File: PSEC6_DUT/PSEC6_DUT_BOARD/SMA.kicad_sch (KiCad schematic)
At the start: 0 parts

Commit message: schematic stuff
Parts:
- added C58, C59, C60, C61, C62, C63, C64, C65, C66, C67, C68, C69, C70, C71, C72, C73: 100n, Capacitor_SMD:C_0603_1608Metric, symbol Device:C_Small
- added J10, J3, J4, J5, J6, J7, J8, J9: Conn_Coaxial, Connector_Coaxial:SMA_Amphenol_132134-14_Vertical, symbol Connector:Conn_Coaxial
- added L1, L2, L3, L4, L5, L6, L7, L8: L, symbol Device:L
- added R50, R51, R52, R53, R54, R55, R56, R57: 50, Resistor_SMD:R_0603_1608Metric, symbol Device:R_Small_US
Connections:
- new net: C70.2, J9.2 (Ext)
- new net: C64.2, J6.2 (Ext)
- new net: C60.2, J4.2 (Ext)
- new net: C67.2, L5.1, R54.2
- new net: C62.2, J5.2 (Ext)
- new net: C59.2, L1.1, R50.2
- new net: C58.2, J3.2 (Ext)
- new net: C69.2, L6.1, R55.2
- new net: C71.2, L7.1, R56.2
- new net: C72.2, J10.2 (Ext)
- new net: C63.2, L3.1, R52.2
- new net: C65.2, L4.1, R53.2
- new net: C61.2, L2.1, R51.2
- new net: C68.2, J8.2 (Ext)
- new net: C73.2, L8.1, R57.2
- new net: C66.2, J7.2 (Ext)
- new net GND: C59.1, C61.1, C63.1, C65.1, C67.1, C69.1, C71.1, C73.1, J10.1 (In), J3.1 (In), J4.1 (In), J5.1 (In), J6.1 (In), J7.1 (In), J8.1 (In), J9.1 (In)
- new net SIGNAL1: C58.1, R50.1
- new net SIGNAL2: C60.1, C72.1, R51.1, R57.1
- new net SIGNAL3: C62.1, R52.1
- new net SIGNAL4: C64.1, R53.1
- new net SIGNAL5: C66.1, R54.1
- new net SIGNAL6: C68.1, R55.1
- new net SIGNAL7: C70.1, R56.1
- new net V_ped1: L1.2
- new net V_ped2: L2.2
- new net V_ped3: L3.2
- new net V_ped4: L4.2
- new net V_ped5: L5.2
- new net V_ped6: L6.2
- new net V_ped7: L7.2
- new net V_ped8: L8.2

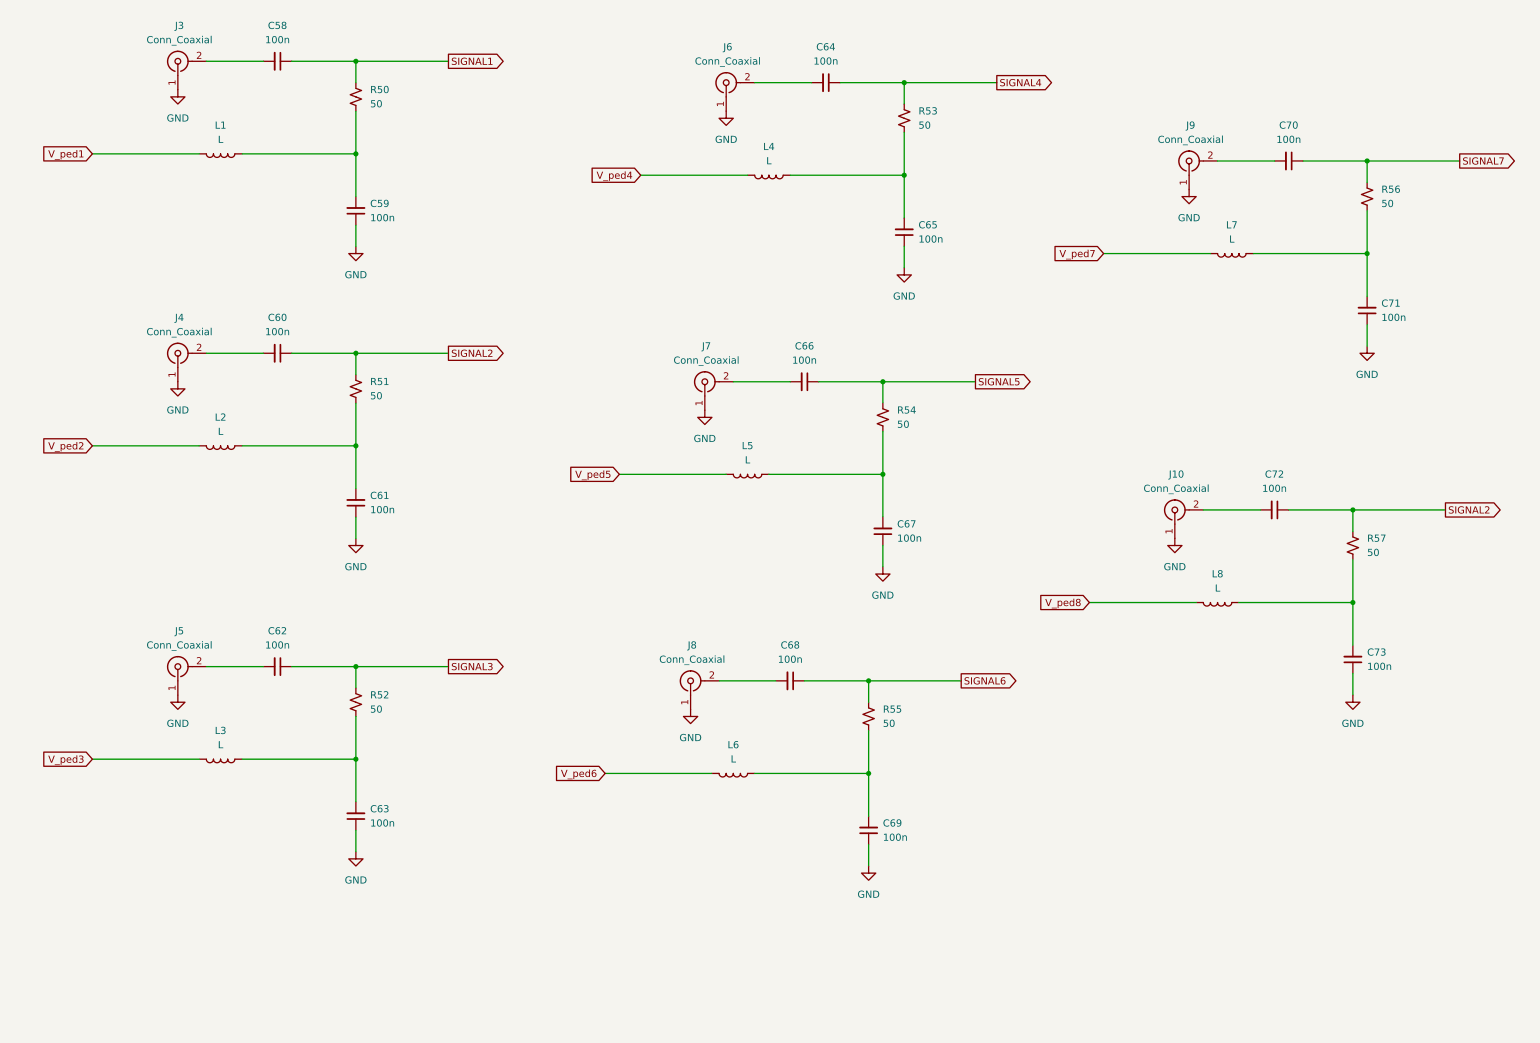
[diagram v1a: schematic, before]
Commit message: Updating values and added RC filters for DUT Card
Added RC filters onto the bias signals and discriminator thresholds, and added RCL values for the SMA devices to provide good DC biasing voltage from the pedestals.
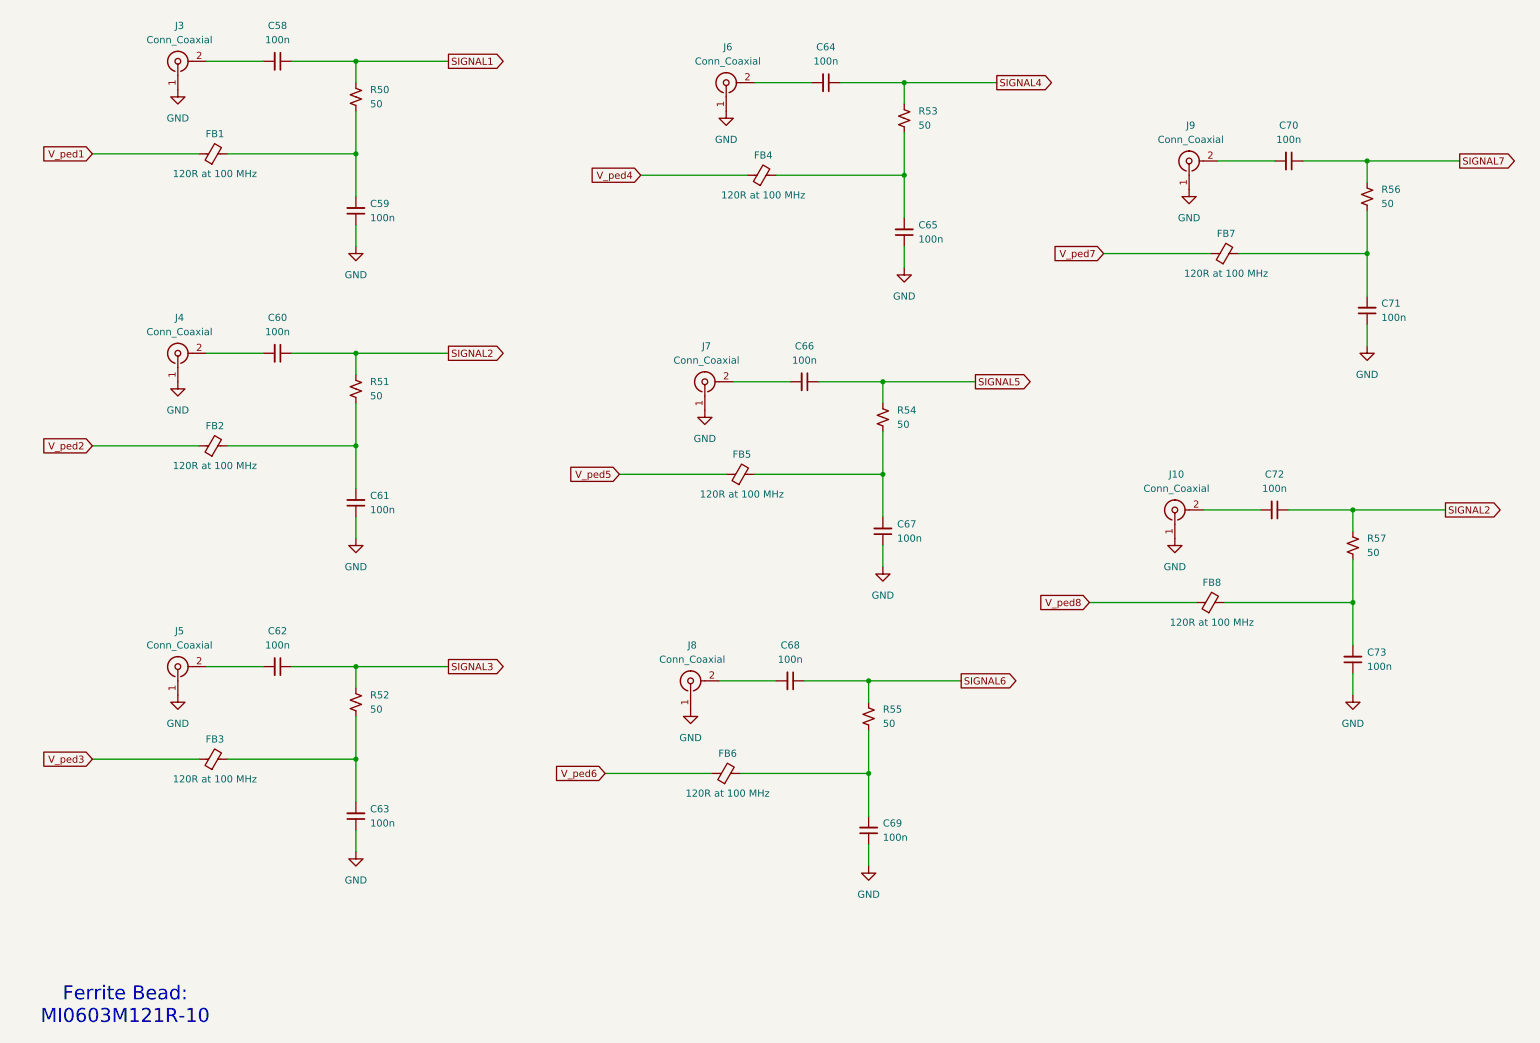
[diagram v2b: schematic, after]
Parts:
- removed L1, L2, L3, L4, L5, L6, L7, L8: L, symbol Device:L
- added FB1, FB2, FB3, FB4, FB5, FB6, FB7, FB8: 120R at 100 MHz, Resistor_SMD:R_0603_1608Metric, symbol Device:FerriteBead_Small
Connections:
- net V_ped1: now also FB1.1
- net V_ped2: now also FB2.1
- net V_ped3: now also FB3.1
- net V_ped4: now also FB4.1
- net V_ped5: now also FB5.1
- net V_ped6: now also FB6.1
- net V_ped7: now also FB7.1
- net V_ped8: now also FB8.1
- net at C67.2, R54.2: now also FB5.2
- net at C59.2, R50.2: now also FB1.2
- net at C69.2, R55.2: now also FB6.2
- net at C71.2, R56.2: now also FB7.2
- net at C63.2, R52.2: now also FB3.2
- net at C65.2, R53.2: now also FB4.2
- net at C61.2, R51.2: now also FB2.2
- net at C73.2, R57.2: now also FB8.2
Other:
- note added: "Ferrite Bead: MI0603M121R-10"

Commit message: DUT Board Schematic Done besides SAMTEC
The DUT Board is now done and fully documented besides the placement of the signals on the SAMTEC connector between the two boards, as the position of each connection will be determined during layout.
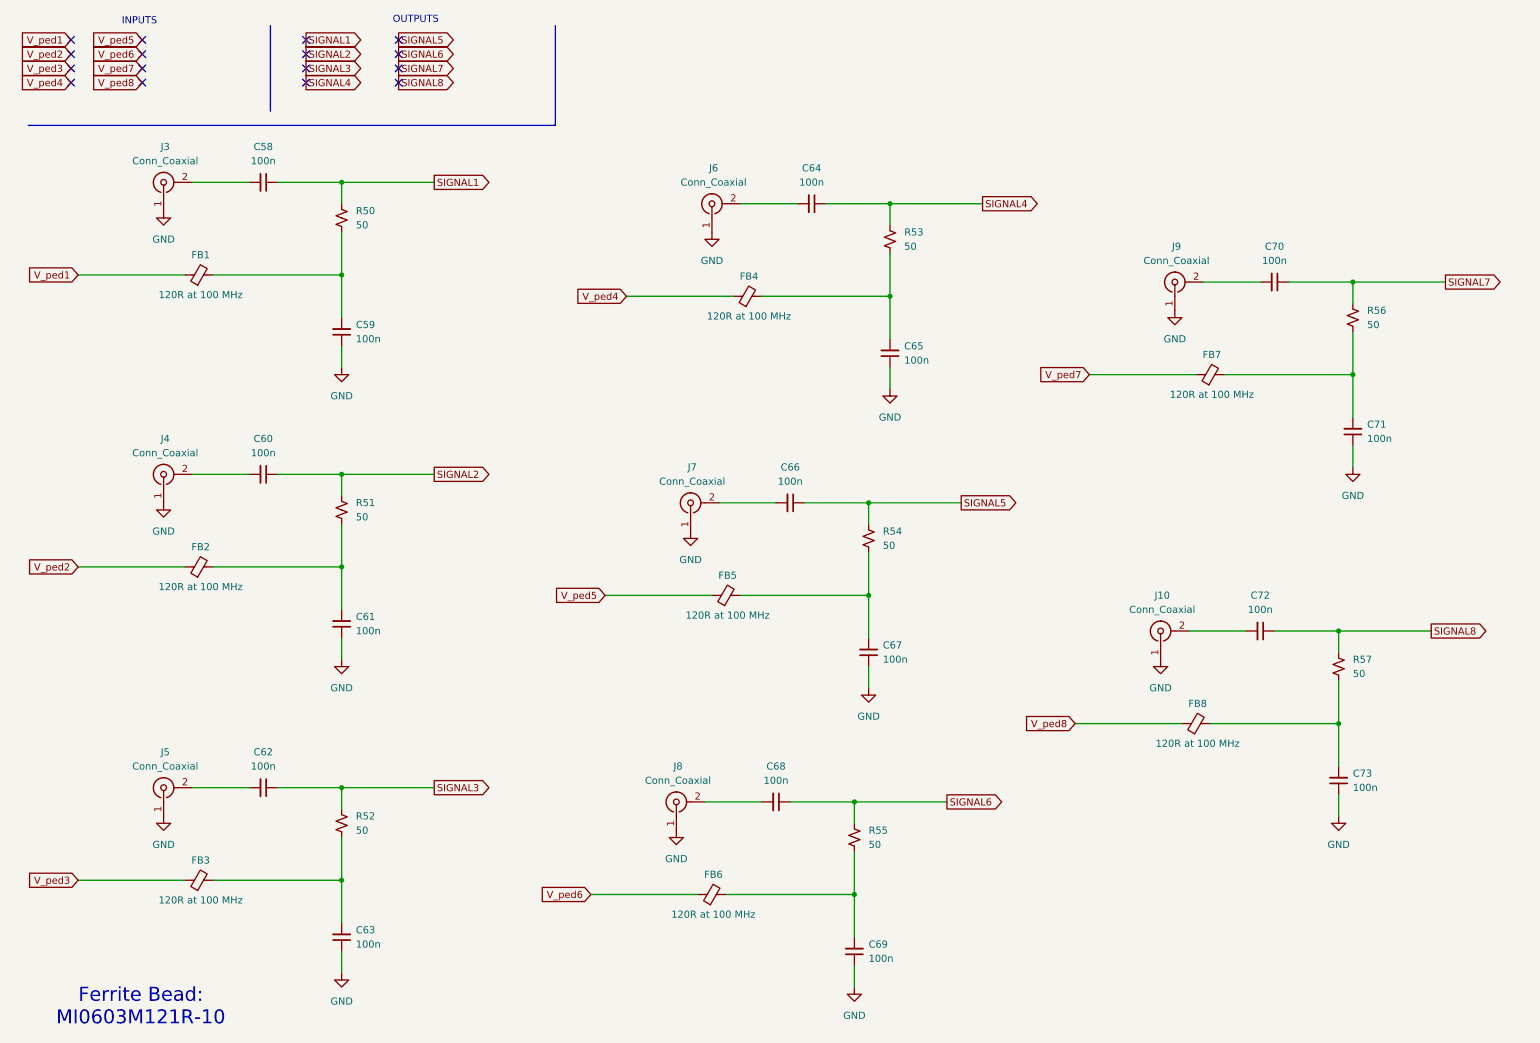
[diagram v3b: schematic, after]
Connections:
- net SIGNAL2: no longer C72.1, R57.1
- new net SIGNAL8: C72.1, R57.1
- no-connect marks 0 -> 16
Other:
- note added: "INPUTS"
- note added: "OUTPUTS"
- moved on the sheet: C58, C59, C60, C61, C62, C63, C64, C65, C66, C67, C68, C69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

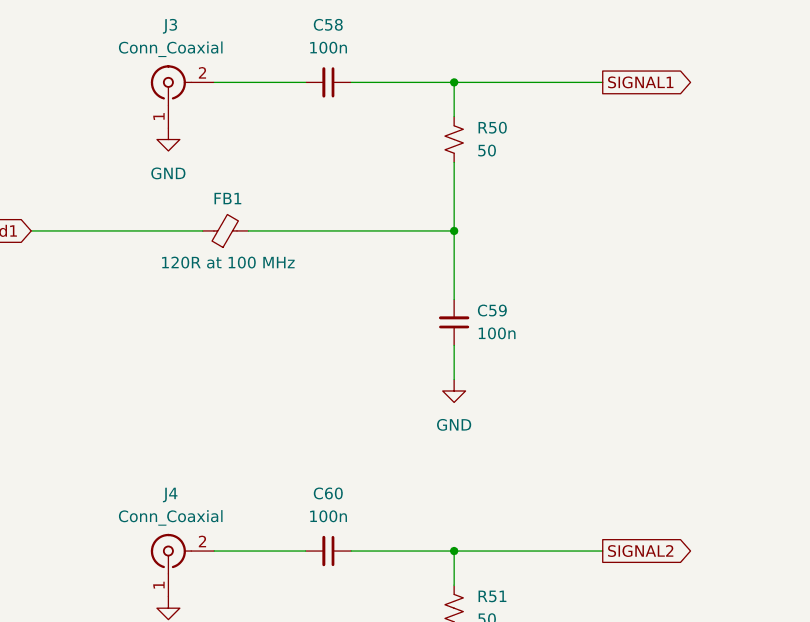
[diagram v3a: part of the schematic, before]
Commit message: Many Updates
Starting new power sequence and implementing KR260 PS circuitry.
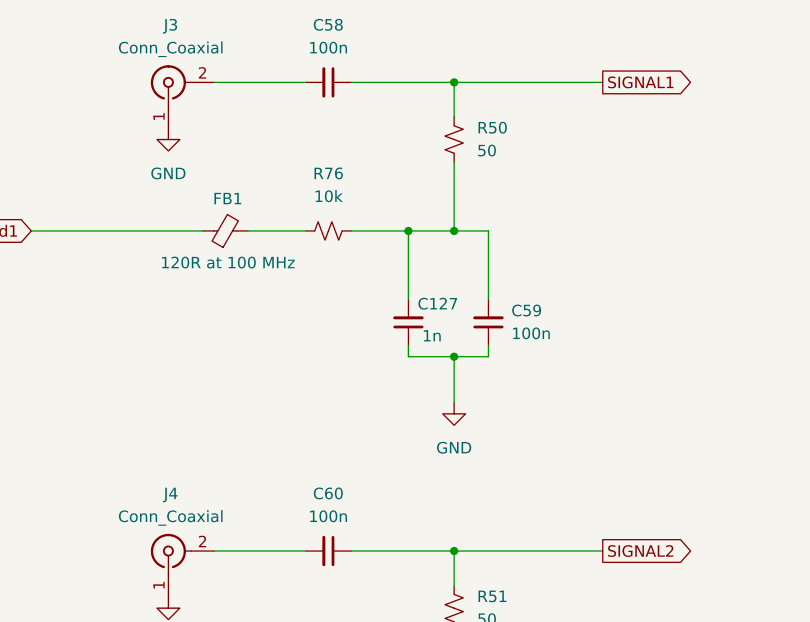
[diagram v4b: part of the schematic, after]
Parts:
- added C127: 1n, Capacitor_SMD:C_0603_1608Metric, symbol Device:C_Small
- added R76: 10k, Resistor_SMD:R_0603_1608Metric, symbol Device:R_Small_US
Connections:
- net GND: now also C127.1
- net at C59.2, R50.2: now also C127.2, R76.2; no longer FB1.2
- new net: FB1.2, R76.1
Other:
- moved on the sheet: C59
